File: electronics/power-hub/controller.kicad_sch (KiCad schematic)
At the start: 55 parts, among them J6 USB, SW1 RESET, SW2 BOOT, U2 LMR51635YDDCR, U3 AP2112K-3.3TRG1, U4 ESP32-S3-MINI-1-N8, U5 USBLC6-2SC6, U6 TJA1462AT

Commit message: Power hub: 47 nF soft start, the LMR51625, the controller sheet on A2
Fixes from the schematic counter-review that the user approved.

* Every 22 nF goes to 47 nF.  The new part is C1622 (basic, the same
  0603 pads).  It covers C21-C24 (eFuse dVdT), C61-C64 (the IMON
  filter, now 47 us) and C118/C119 (the CAN split terminations).
  - A row of four nodes is about 450 uF.  With 22 nF the soft start
    charged it at about 2.6 A, over the 1.6 A limit.
  - With 47 nF it charges at about 1.2 A.  The ramp is 7.5 ms at 20 V
    and 10.5 ms at 28 V (t = 8e3 x V_IN x C_dVdT).
  - passives.py and its cache gain the 47 nF.
* The hub firmware's FLT blanking goes from 10 ms to 25 ms
  (HUB_ROW_FLT_BLANK_MS).  The TPS2660 asserts FLT through its soft
  start, and at 28 V that start now lasts 10.5 ms, longer than 10 ms.
* The buck changes from the LMR51635 to the LMR51625 with the 4.7 uH
  FXL0630-4R7-M.  These are the node's pair (buck25 / buck_l47, TI
  SLUSF64B table 8-1).
  - The controller takes under 0.7 A.
  - Same pinout and footprint, so the same 270 deg CPL correction.
* The routed PCB keeps its routing.  Only the properties of those 12
  footprints change (value, MPN, LCSC, description, datasheet).  They
  were copied from design.py with KiCad's Python, as pcbgen places
  them.
* The controller sheet (page 4) goes on A2, so the CAN block, the
  mounting holes and the notes are now on the page.
* Stale notes corrected:
  - the charger: 100 W at 20 V by default, 140 W EPR as an option;
  - the TPS26600's internal OVP is 31-34 V (typ 32.6 V), not 33 V
    (design.py, power.md, the devicetree comment);
  - the buck block now reads "from VRACK": there is no input switch
    any more.

Regenerated on zephyrbox with kicad.sh power-hub --check --fab.
- ERC 0, DRC 0, unconnected 0, parity 0.
- The Gerber zip and the top and iso renders are the same content.
  The bottom render's only difference was 9 pixels of raytracer
  noise in via holes, so it is kept.
- The viewer GLB com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
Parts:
- C118, C119: value 22n -> 47n; LCSC C21122 -> C1622; MPN CL10B223KB8NNNC -> CL10B473KB8NNNC
- L1: value 3.3u -> 4.7u; LCSC C167219 -> C167220; MPN FXL0630-3R3-M -> FXL0630-4R7-M
- U2: value LMR51635YDDCR -> LMR51625YDDCR; Alternative LMR51635YFDDCR (C44750836): same, forced PWM, no spread spe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 -> LMR51625YFDDCR (C45262768): same, forced PWM, no spread spe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; LCSC C45262770 -> C44991044; MPN LMR51635YDDCR -> LMR51625YDDCR
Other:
- note added: "5 V buck: LMR51625 (2.5 A; the controller takes < 0.7 A) and 4.7 µH, as the bay node (TI SLUSF64B table 8-1), from VRACK"
- note removed: "5 V buck: LMR51635, as the bay node (TI SLUSF64B table 8-2), from VBUS ahead of the switch"
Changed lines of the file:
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@@
 	(generator "hw-testing-rack-eda")
 	(generator_version "10.0")
-	(paper "A3")
+	(paper "A2")
 	(title_block
 		(title "Power hub — Rack controller: supplies, ESP32-S3, USB-C, CAN")
@@
 		(comment 2 "Generated from electronics/power-hub/design.py — edit the Python, then regenerate")
 	)
-	(text "5 V buck: LMR51635, as the bay node (TI SLUSF64B table 8-2), from VBUS ahead of the switch"
+	(text "5 V buck: LMR51625 (2.5 A; the controller takes < 0.7 A) and 4.7 µH, as the bay node (TI SLUSF64B table 8-1), from VRACK"
 		(exclude_from_sim no)
 		(at 20.32 30.48 0)
@@
 			)
 		)
-		(property "Value" "LMR51635YDDCR"
+		(property "Value" "LMR51625YDDCR"
 			(at 106.68 55.88 0)
 			(effects
@@
 			)
 		)
-		(property "Datasheet" "https://www.ti.com/lit/ds/symlink/lmr51635.pdf"
+		(property "Datasheet" "https://www.ti.com/lit/ds/symlink/lmr51625.pdf"
 			(at 106.68 46.99 0)
 			(effects
@@
 			)
 		)
-		(property "Description" "4.3–60 V 3.5 A synchronous buck, 1.1 MHz, PFM + spread spectrum"
+		(property "Description" "4.3–60 V 2.5 A synchronous buck, 1.1 MHz, PFM + spread spectrum"
 			(at 106.68 46.99 0)
 			(effects
@@
 			)
 		)
-		(property "MPN" "LMR51635YDDCR"
+		(property "MPN" "LMR51625YDDCR"
 			(at 106.68 46.99 0)
 			(effects
@@
 			)
 		)
-		(property "LCSC" "C45262770"
+		(property "LCSC" "C44991044"
 			(at 106.68 46.99 0)
 			(effects
@@
 			)
 		)
-		(property "Alternative" "LMR51635YFDDCR (C44750836): same, forced PWM, no spread spectrum"
+		(property "Alternative" "LMR51625YFDDCR (C45262768): same, forced PWM, no spread spectrum; LMR51635YDDCR (C45262770): 3.5 A, 3.3 µH"
 			(at 106.68 46.99 0)
 			(effects
@@
 			)
 		)
-		(property "Value" "3.3u"
+		(property "Value" "4.7u"
 			(at 152.4 48.26 0)
 			(effects
@@
 			)
 		)
-		(property "Description" "3.3 µH, 9.5 A sat, 8.5 A rms, 22 mΩ, molded"
+		(property "Description" "4.7 µH, 9 A sat, 6 A rms, 33 mΩ, molded"
 			(at 151.13 50.8 0)
 			(effects
@@
 			)
 		)
-		(property "MPN" "FXL0630-3R3-M"
+		(property "MPN" "FXL0630-4R7-M"
 			(at 151.13 50.8 0)
 			(effects
@@
 			)
 		)
-		(property "LCSC" "C167219"
+		(property "LCSC" "C167220"
 			(at 151.13 50.8 0)
 			(effects
@@
 			)
 		)
-		(property "Value" "22n"
+		(property "Value" "47n"
 			(at 97.79 334.01 0)
 			(effects
@@
 			)
 		)
-		(property "Description" "Capacitor 22n 0603"
+		(property "Description" "Capacitor 47n 0603"
 			(at 93.98 336.55 0)
 			(effects
@@
 			)
 		)
-		(property "LCSC" "C21122"
+		(property "LCSC" "C1622"
 			(at 93.98 336.55 0)
 			(effects
@@
 			)
 		)
-		(property "MPN" "CL10B223KB8NNNC"
+		(property "MPN" "CL10B473KB8NNNC"
 			(at 93.98 336.55 0)
 			(effects
@@
 			)
 		)
-		(property "Value" "22n"
+		(property "Value" "47n"
 			(at 107.95 334.01 0)
 			(effects
@@
 			)
 		)
-		(property "Description" "Capacitor 22n 0603"
+		(property "Description" "Capacitor 47n 0603"
 			(at 104.14 336.55 0)
 			(effects
@@
 			)
 		)
-		(property "LCSC" "C21122"
+		(property "LCSC" "C1622"
 			(at 104.14 336.55 0)
 			(effects
@@
 			)
 		)
-		(property "MPN" "CL10B223KB8NNNC"
+		(property "MPN" "CL10B473KB8NNNC"
 			(at 104.14 336.55 0)
 			(effects
@@
 		)
 	)
-	(text_box "GPIO: IO1/2/4/5 IMON A–D, IO6 VBUS_SENSE (ADC1) · IO7/8/9 CAN TX/RX/STB · IO10–13 POS A–D ·\n  IO14–17 ROW_EN A–D · IO18/21/47/33 FLT A–D · IO39 PD_INT, IO40/41 PD_SCL/SDA, IO42 I2C_PU · IO35 CTL LED ·\n  IO19/20 USB.  Strapping IO3/45/46 unused.\nTermination: two split 2 × 56 Ω + 22 nF (56 Ω in all) at the star centre; nodes carry none.\n+5V: buck (5.24 V; ≈ 4.8 V in dropout on a 5 V contract) or USB VBUS through B5819W Schottkys;\n  AP2112K (250 mV dropout) keeps 3.3 V down to a 5 V contract.  The TJA1462AT wants 4.5–5.5 V: CAN runs once VRACK is up."
+	(text_box "GPIO: IO1/2/4/5 IMON A–D, IO6 VBUS_SENSE (ADC1) · IO7/8/9 CAN TX/RX/STB · IO10–13 POS A–D ·\n  IO14–17 ROW_EN A–D · IO18/21/47/33 FLT A–D · IO39 PD_INT, IO40/41 PD_SCL/SDA, IO42 I2C_PU · IO35 CTL LED ·\n  IO19/20 USB.  Strapping IO3/45/46 unused.\nTermination: two split 2 × 56 Ω + 47 nF (56 Ω in all) at the star centre; nodes carry none.\n+5V: buck (5.24 V; ≈ 4.8 V in dropout on a 5 V contract) or USB VBUS through B5819W Schottkys;\n  AP2112K (250 mV dropout) keeps 3.3 V down to a 5 V contract.  The TJA1462AT wants 4.5–5.5 V: CAN runs once VRACK is up."
 		(exclude_from_sim no)
 		(at 20.32 386.08 0)
-		(size 240.03 17.78)
+		(size 414.02 17.78)
 		(margins 1.5 1.5 1.5 1.5)
 		(stroke

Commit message: Datasheet audit F1-F6: the pod's AP2114H, STB 5.1k, PC_DET hysteresis, the camera ESD's 100 nF, the eFuse step
The user approved the audit's fixes for the node, the hub and the pod
("Go pour 1"); docs/datasheet-audit.md marks F1-F6 applied.

* F1, camera pod: U1 AMS1117-3.3 -> AP2114H-3.3TRG1 (C150716, catalog
  ldo_1a, the node's U2).
  - The AMS1117 is specified stable only with 22 uF tantalum; the
    AP2114H is stable with the ceramic C2.
  - Same SOT-223 pinout, copper (the +3V3 pour and island round the
    tab stay) and 180 deg CPL correction.
  - One more extended type on the pod's Economic order: +$3.09 and
    $0.05 of parts (JLC_SINCE_QUOTE).
* F2, power hub: R214 (TJA1462 STB pull-down) 10k -> 5.1k (C23186,
  already on the board). With IO9 floating, STB's internal pull-up
  (20 kOhm minimum) left it at up to 1.10 V, over VIL 0.99 V.
* F3, bay node: R42 150k from MUX_SEL back to PC_DET, beside U7 (C22807,
  on the board since S1).
  - The laptop's VBUS rises at ~50 us/V through R11/R12, where the
    LVC1G32 wants <= 10 ns/V and warns of oscillation.
  - This gives ~0.14 V of hysteresis.
* F4, bay node: C28 100 nF (C14663) on U12/U13's VBUS pins (+3V3), above
  U12 by its pin 5. Between the two ICs their courtyards leave no room.
* F5, node and hub: firmware.md's first-flash procedure gains the
  irreversible DIS_USB_OTG_DOWNLOAD_MODE eFuse step. In USB-OTG
  download boot the ROM drives IO40 high: the node's DUT_FLT_N, the
  hub's PD_SCL. Nothing is burnt.
* F6, notes, hub:
  - the IMON filter is 0.9 ms, not 47 us: the pin is a current source;
  - the buck stops at ~3.8 V (internal UVLO);
  - SHDN turns on at >= 1 V;
  - the soft start stays under the limit only typically;
  - the CH224A note follows CH224 V2.1: the source PDOs are listed for
    both parts and readable under 100 W, which is still to check with
    ours (review R3); single-byte transfers; no "same die".
* F6, notes, node: TPS2553D; the LDO's 1.94 V x 0.4 A ~ 0.8 W; L1's
  7.5 A guarante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
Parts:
- R214: value 10k -> 5.1k; LCSC C25804 -> C23186; MPN 0603WAF1002T5E -> 0603WAF5101T5E
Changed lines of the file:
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@@
 			)
 		)
-		(property "Description" "4.7 µH, 9 A sat, 6 A rms, 33 mΩ, molded"
+		(property "Description" "4.7 µH, 7.5 A sat (9 A typ), 5.5 A rms, 33 mΩ, molded"
 			(at 151.13 50.8 0)
 			(effects
@@
 			)
 		)
-		(property "Value" "10k"
+		(property "Value" "5.1k"
 			(at 33.02 323.85 0)
 			(effects
@@
 			)
 		)
-		(property "Description" "Resistor 10k 0603"
+		(property "Description" "Resistor 5.1k 0603"
 			(at 30.48 326.39 0)
 			(effects
@@
 			)
 		)
-		(property "LCSC" "C25804"
+		(property "LCSC" "C23186"
 			(at 30.48 326.39 0)
 			(effects
@@
 			)
 		)
-		(property "MPN" "0603WAF1002T5E"
+		(property "MPN" "0603WAF5101T5E"
 			(at 30.48 326.39 0)
 			(effects

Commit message: Boards: labelled bottom test pads; hub dVdT 100 nF, 50 ms FLT blank
Eve's DFT rule on the four boards this session owns: bare pads on the
bottom, named on B.SilkS, out of the BOM and the CPL (no part, no
assembly fee).  Supply pads 1.5 mm, signal pads 1.0 mm (new catalog
entry "testpad1"), all more than 2 mm from any THT pad or hole
(closest: 4.7 mm, the pod's TP4).  Positions are fixed in design.py,
so they stay put across revisions.

- bay node, 17: TX, RX, 3V3, GND by the module (kept), then EN, IO0,
  FLT (DUT_FLT_N), ALRT (INA_ALERT_N), SDA, SCL and a second GND;
  a supply row along the bottom edge: GND, VIN, 5V, 3V3, DUT 5V,
  CAM 5V
- power hub, 20: TX, RX, 3V3, GND, 5V, VRACK, GND (kept), then EN,
  IO0, the CH224A's PD SDA/SCL, each row's FLT and IMON (A-D) and a
  third GND in the middle
- camera pod, 4: GND, 5V, 3V3 and a second GND at the far end
- DATA port, 2: GND and 5V (VBUS, through a via under its track)

Hub, as the datasheet audit's U1 answer asks (TPS2660 Fig. 55 at
85 C: 8-10 ms at 21 W fails the 47 nF worst start, 33 ms at 14 W
covers 100 nF): C21-C24 dVdT 47 nF -> 100 nF, so a row's soft start
is 16-22 ms and dissipates about 7-9 W typical, 14 W worst, for
19-24 ms; the firmware's HUB_ROW_FLT_BLANK_MS goes 25 -> 50 ms to
cover it (worst case 39 ms).  docs/power.md, the audit row and the
hub notes say so.

Routing fallout: J1's A12/B1 GND now leaves through one drawn 0.5 mm
via so the automatic fan-out can't cut the VRACK pour off A9/B4; the
pod's LDO tab zones are exclusive so tracks no longer split them.

All four rerouted, tidied and checked: ERC 0, DRC 0, unconnected 0,
parity 0.  Gerbers, renders, schematics, viewer GLBs, the JLC
snapshot lines and the rack BOM regenerated.

Co-Authored-By: Claude Opus 5.5 <noreply@anthropic.com>
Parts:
- added TP10: PD_SDA, TestPoint:TestPoint_Pad_D1.0mm, symbol Connector:TestPoint
- added TP11: PD_SCL, TestPoint:TestPoint_Pad_D1.0mm, symbol Connector:TestPoint
- added TP12: FLT_A, TestPoint:TestPoint_Pad_D1.0mm, symbol Connector:TestPoint
- added TP13: ADC_IMON_A, TestPoint:TestPoint_Pad_D1.0mm, symbol Connector:TestPoint
- added TP14: FLT_B, TestPoint:TestPoint_Pad_D1.0mm, symbol Connector:TestPoint
- added TP15: ADC_IMON_B, TestPoint:TestPoint_Pad_D1.0mm, symbol Connector:TestPoint
- added TP16: FLT_C, TestPoint:TestPoint_Pad_D1.0mm, symbol Connector:TestPoint
- added TP17: ADC_IMON_C, TestPoint:TestPoint_Pad_D1.0mm, symbol Connector:TestPoint
- added TP18: FLT_D, TestPoint:TestPoint_Pad_D1.0mm, symbol Connector:TestPoint
- added TP19: ADC_IMON_D, TestPoint:TestPoint_Pad_D1.0mm, symbol Connector:TestPoint
- added TP20: GND, TestPoint:TestPoint_Pad_D1.5mm, symbol Connector:TestPoint
- added TP8: EN, TestPoint:TestPoint_Pad_D1.0mm, symbol Connector:TestPoint
- added TP9: BOOT, TestPoint:TestPoint_Pad_D1.0mm, symbol Connector:TestPoint
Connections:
- net ADC_IMON_A: now also TP13.1
- net ADC_IMON_B: now also TP15.1
- net ADC_IMON_C: now also TP17.1
- net ADC_IMON_D: now also TP19.1
- net BOOT: now also TP9.1
- net EN: now also TP8.1
- net FLT_A: now also TP12.1
- net FLT_B: now also TP14.1
- net FLT_C: now also TP16.1
- net FLT_D: now also TP18.1
- net GND: now also TP20.1
- net PD_SCL: now also TP11.1
- net PD_SDA: now also TP10.1
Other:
- moved on the sheet: C116, C117, C118, C119, C120, D9, H1, H2, H3, H4, J6, R212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

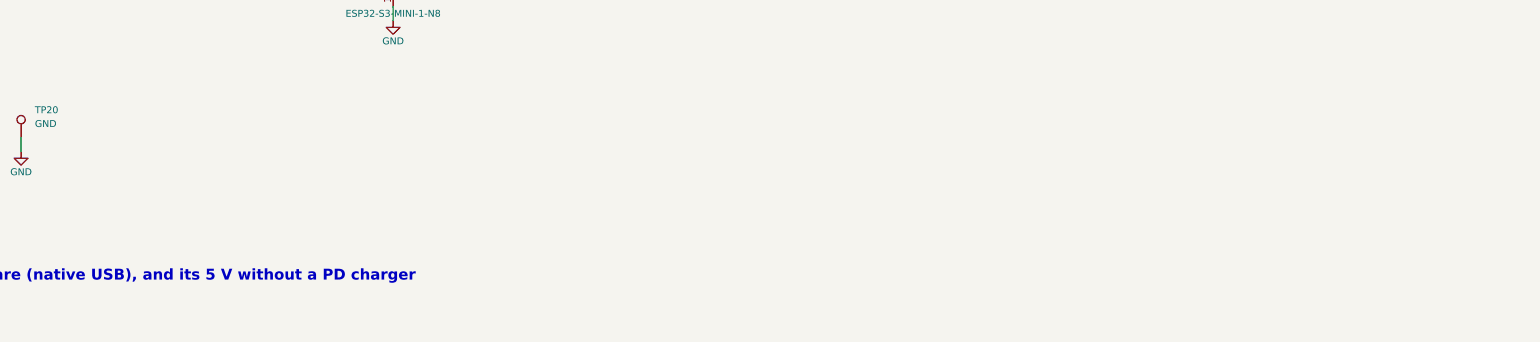
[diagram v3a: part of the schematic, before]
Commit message: Power hub: 18 more labelled bottom test pads (PH-2)
The kicad-happy review's PH-2, against Eve's rule: three bring-up
checks had no probe point (the +5V_BUCK load step, a row's output
during a short, the CAN common mode).  TP21-TP38, bare pads on B.Cu
named on B.SilkS, out of the BOM and the CPL:
- 1.5 mm: 5V BUCK, USB 5V, VHV (the CH224A's), ROW A-D, and a GND by
  the CAN pads;
- 1.0 mm: PD PG (PD_INT), CANH, CANL, TXD, RXD, EN A-D (ROW_EN), VSNS
  (VBUS_SENSE).

Each pad sits where its net already is, so no routing moves:
- 7 on a new drawn via, on one of the net's F.Cu track bends or in
  its pour (5V BUCK, USB 5V, VHV, PD PG, TXD, RXD, GND);
- 5 on a via the router had put there, now drawn so it stays
  (CANH, EN A-D);
- the 4 rows on their own drawn output vias;
- 2 on the end of a B.Cu track (CANL, VSNS).
None adds a via on In2's VRACK band.  All are at least 2 mm from any
through-hole pad or hole, and 2.7 mm from each other.  The GND pad
gets the usual GND fan-out to In1.  Positions are in TP_ROUND2 in
design.py.

Every track and via is the previous commit's, but those.  ERC 0,
DRC 0, unconnected 0, parity 0.

Co-Authored-By: Claude Opus 5.5 <noreply@anthropic.com>
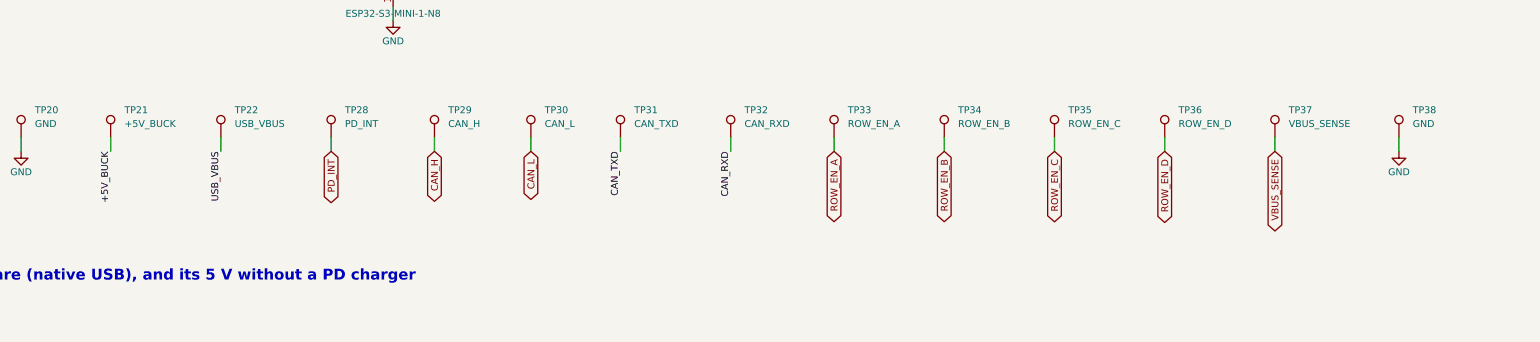
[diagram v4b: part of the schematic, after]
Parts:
- added TP21: +5V_BUCK, TestPoint:TestPoint_Pad_D1.5mm, symbol Connector:TestPoint
- added TP22: USB_VBUS, TestPoint:TestPoint_Pad_D1.5mm, symbol Connector:TestPoint
- added TP28: PD_INT, TestPoint:TestPoint_Pad_D1.0mm, symbol Connector:TestPoint
- added TP29: CAN_H, TestPoint:TestPoint_Pad_D1.0mm, symbol Connector:TestPoint
- added TP30: CAN_L, TestPoint:TestPoint_Pad_D1.0mm, symbol Connector:TestPoint
- added TP31: CAN_TXD, TestPoint:TestPoint_Pad_D1.0mm, symbol Connector:TestPoint
- added TP32: CAN_RXD, TestPoint:TestPoint_Pad_D1.0mm, symbol Connector:TestPoint
- added TP33: ROW_EN_A, TestPoint:TestPoint_Pad_D1.0mm, symbol Connector:TestPoint
- added TP34: ROW_EN_B, TestPoint:TestPoint_Pad_D1.0mm, symbol Connector:TestPoint
- added TP35: ROW_EN_C, TestPoint:TestPoint_Pad_D1.0mm, symbol Connector:TestPoint
- added TP36: ROW_EN_D, TestPoint:TestPoint_Pad_D1.0mm, symbol Connector:TestPoint
- added TP37: VBUS_SENSE, TestPoint:TestPoint_Pad_D1.0mm, symbol Connector:TestPoint
- added TP38: GND, TestPoint:TestPoint_Pad_D1.5mm, symbol Connector:TestPoint
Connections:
- net +5V_BUCK: now also TP21.1
- net CAN_H: now also TP29.1
- net CAN_L: now also TP30.1
- net CAN_RXD: now also TP32.1
- net CAN_TXD: now also TP31.1
- net GND: now also TP38.1
- net PD_INT: now also TP28.1
- net ROW_EN_A: now also TP33.1
- net ROW_EN_B: now also TP34.1
- net ROW_EN_C: now also TP35.1
- net ROW_EN_D: now also TP36.1
- net USB_VBUS: now also TP22.1
- net VBUS_SENSE: now also TP37.1
